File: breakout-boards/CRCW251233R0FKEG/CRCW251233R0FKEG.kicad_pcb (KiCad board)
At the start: 2 copper layers, 14 parts, among them J1 Conn_01x12, J2 Conn_01x12

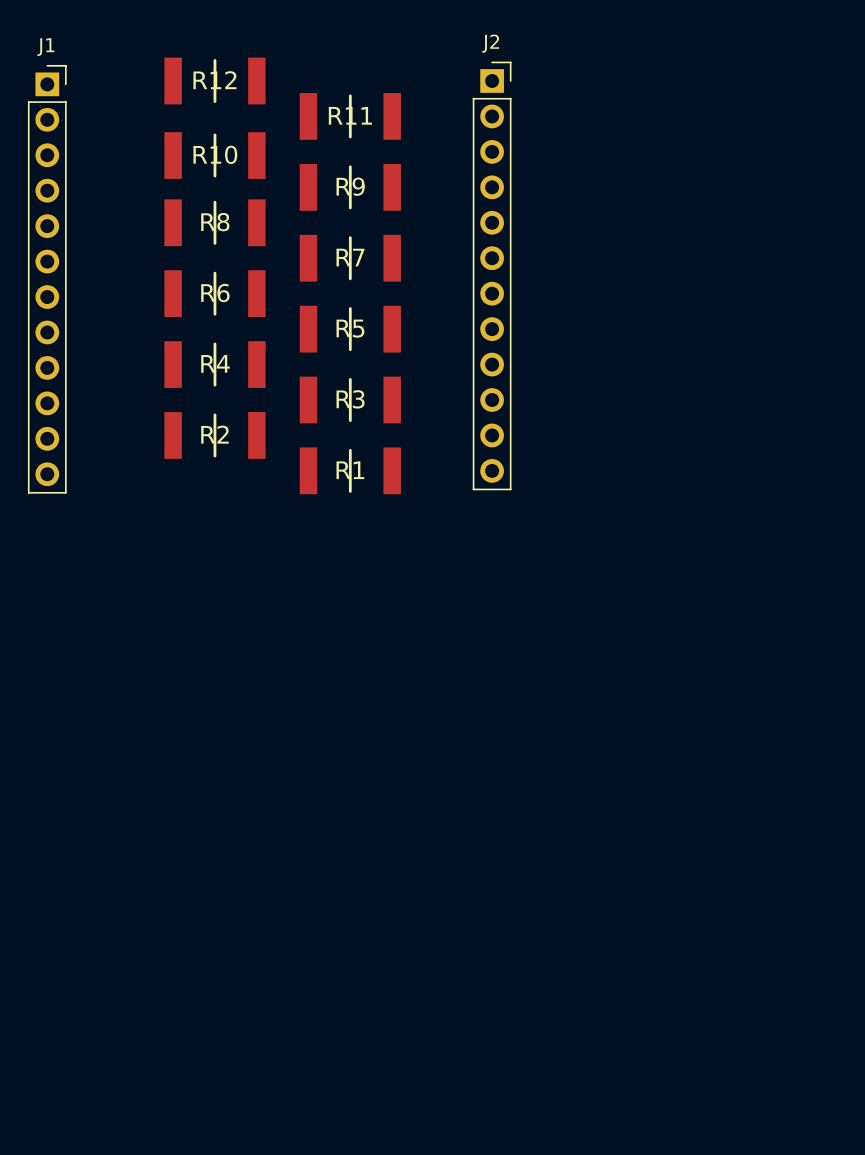
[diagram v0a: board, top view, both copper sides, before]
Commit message: fix: change board alignement
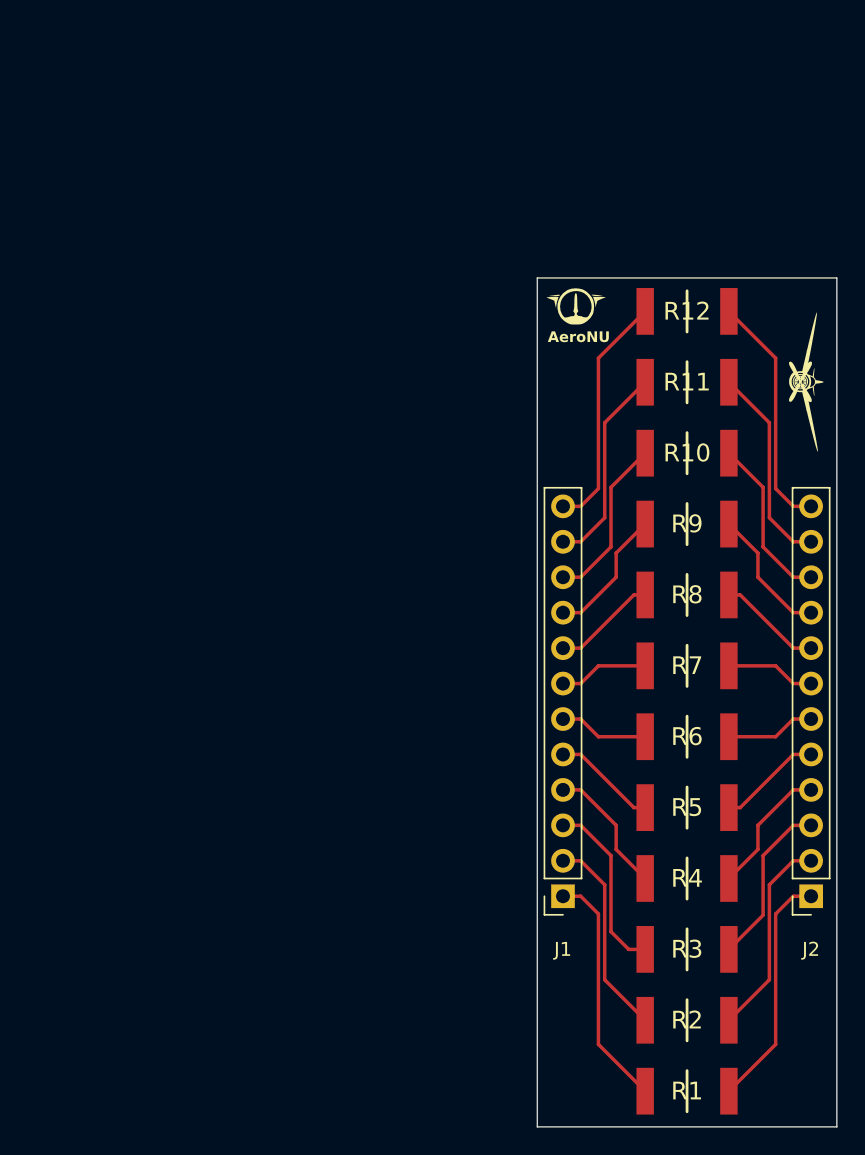
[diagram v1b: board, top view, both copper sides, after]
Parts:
- added AeroNU: LOGO, FixedWing:AeroNU - Logo (Smol), F.Cu at (153.5, 64.6)
- added FixedWing: LOGO, FixedWing:FixedWing - Logo (Smol), F.Cu at (169.2, 67.3)
- moved J1 68.9 mm to (152.4, 104.1), turned to 180 degrees
- moved J2 62.7 mm to (170.2, 104.1), turned to 180 degrees
- moved R2 53.9 mm to (161.3, 113.0)
- moved R1 50.6 mm to (161.3, 118.1)
- moved R4 50.0 mm to (161.3, 102.9)
- moved R6 46.4 mm to (161.3, 92.7)
- moved R3 46.2 mm to (161.3, 108.0)
- moved R8 43.1 mm to (161.3, 82.5)
- moved R5 41.9 mm to (161.3, 97.8)
- moved R10 40.0 mm to (161.3, 72.4)
- moved R7 37.9 mm to (161.3, 87.6)
- moved R12 37.6 mm to (161.3, 62.2)
- moved R9 34.1 mm to (161.3, 77.5)
- moved R11 30.7 mm to (161.3, 67.3)
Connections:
- R1 pad 1: Net-(J1-Pin_12) -> Net-(J1-Pin_1)
- R1 pad 2: Net-(J2-Pin_12) -> Net-(J2-Pin_1)
- R10 pad 1: Net-(J1-Pin_3) -> Net-(J1-Pin_10)
- R10 pad 2: Net-(J2-Pin_3) -> Net-(J2-Pin_10)
- R11 pad 1: Net-(J1-Pin_2) -> Net-(J1-Pin_11)
- R11 pad 2: Net-(J2-Pin_2) -> Net-(J2-Pin_11)
- R12 pad 1: Net-(J1-Pin_1) -> Net-(J1-Pin_12)
- R12 pad 2: Net-(J2-Pin_1) -> Net-(J2-Pin_12)
- R2 pad 1: Net-(J1-Pin_11) -> Net-(J1-Pin_2)
- R2 pad 2: Net-(J2-Pin_11) -> Net-(J2-Pin_2)
- R3 pad 1: Net-(J1-Pin_10) -> Net-(J1-Pin_3)
- R3 pad 2: Net-(J2-Pin_10) -> Net-(J2-Pin_3)
- R4 pad 1: Net-(J1-Pin_9) -> Net-(J1-Pin_4)
- R4 pad 2: Net-(J2-Pin_9) -> Net-(J2-Pin_4)
- R5 pad 1: Net-(J1-Pin_8) -> Net-(J1-Pin_5)
- R5 pad 2: Net-(J2-Pin_8) -> Net-(J2-Pin_5)
- R6 pad 1: Net-(J1-Pin_7) -> Net-(J1-Pin_6)
- R6 pad 2: Net-(J2-Pin_7) -> Net-(J2-Pin_6)
- R7 pad 1: Net-(J1-Pin_6) -> Net-(J1-Pin_7)
- R7 pad 2: Net-(J2-Pin_6) -> Net-(J2-Pin_7)
- R8 pad 1: Net-(J1-Pin_5) -> Net-(J1-Pin_8)
- R8 pad 2: Net-(J2-Pin_5) -> Net-(J2-Pin_8)
- R9 pad 1: Net-(J1-Pin_4) -> Net-(J1-Pin_9)
- R9 pad 2: Net-(J2-Pin_4) -> Net-(J2-Pin_9)
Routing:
- net Net-(J2-Pin_12): track 0.00 -> 17.2 mm
- net Net-(J2-Pin_1): track 0.00 -> 17.2 mm
- net Net-(J1-Pin_12): track 0.00 -> 17.2 mm
- net Net-(J1-Pin_1): track 0.00 -> 17.2 mm
- net Net-(J2-Pin_2): track 0.00 -> 14.6 mm
- net Net-(J2-Pin_11): track 0.00 -> 14.6 mm
- net Net-(J1-Pin_2): track 0.00 -> 14.6 mm
- net Net-(J1-Pin_11): track 0.00 -> 14.6 mm
- net Net-(J1-Pin_3): track 0.00 -> 12.8 mm
- net Net-(J2-Pin_3): track 0.00 -> 12.1 mm
- net Net-(J2-Pin_10): track 0.00 -> 12.1 mm
- net Net-(J1-Pin_10): track 0.00 -> 12.1 mm
- net Net-(J2-Pin_4): track 0.00 -> 9.53 mm
- net Net-(J2-Pin_9): track 0.00 -> 9.53 mm
- net Net-(J1-Pin_4): track 0.00 -> 9.53 mm
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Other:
- board outline added: 21.5 x 60.8 mm
- board text added: "AeroNU"
- board text added: "Designed By Ephram CJ and Matthew F"

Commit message: feat: finalize 33ohm board design
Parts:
- removed the FixedWing at (169.2, 67.3)
- added FixedWing: LOGO, FixedWing Symbols:FixedWing - Logo (Smol), F.Cu at (169.2, 67.1)
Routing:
- net Net-(J2-Pin_12): track 17.2 -> 18.5 mm
- net Net-(J1-Pin_12): track 17.2 -> 18.5 mm
- net Net-(J2-Pin_11): track 14.6 -> 15.9 mm
- net Net-(J2-Pin_3): track 12.1 -> 13.3 mm
- net Net-(J1-Pin_11): track 14.6 -> 15.8 mm
- net Net-(J1-Pin_1): track 17.2 -> 18.4 mm
- net Net-(J2-Pin_10): track 12.1 -> 13.1 mm
- net Net-(J2-Pin_1): track 17.2 -> 18.2 mm
- net Net-(J1-Pin_10): track 12.1 -> 13.1 mm
- net Net-(J1-Pin_2): track 14.6 -> 15.7 mm
- net Net-(J1-Pin_4): track 9.53 -> 10.6 mm
- net Net-(J2-Pin_5): track 7.47 -> 8.51 mm
- net Net-(J2-Pin_2): track 14.6 -> 15.6 mm
- net Net-(J2-Pin_4): track 9.53 -> 10.5 mm
- net Net-(J2-Pin_9): track 9.53 -> 10.5 mm
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
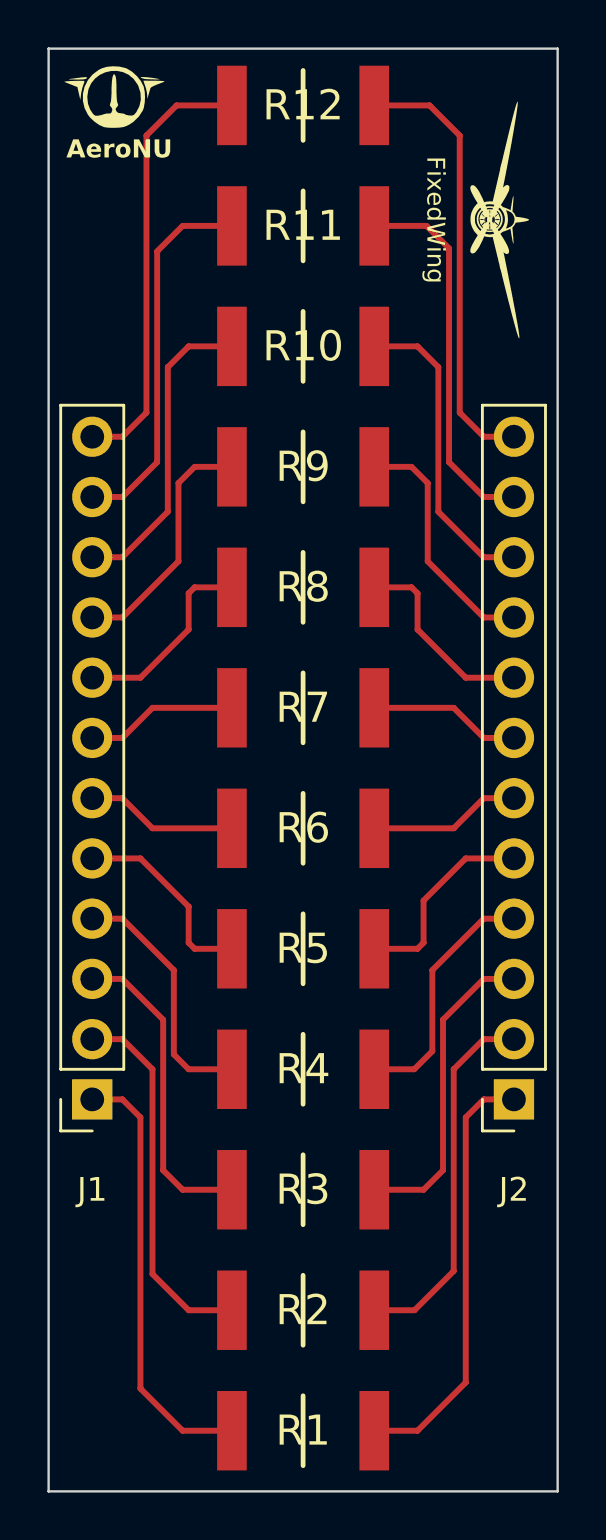
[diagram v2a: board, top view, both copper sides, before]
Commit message: feat: add fillets to all boards
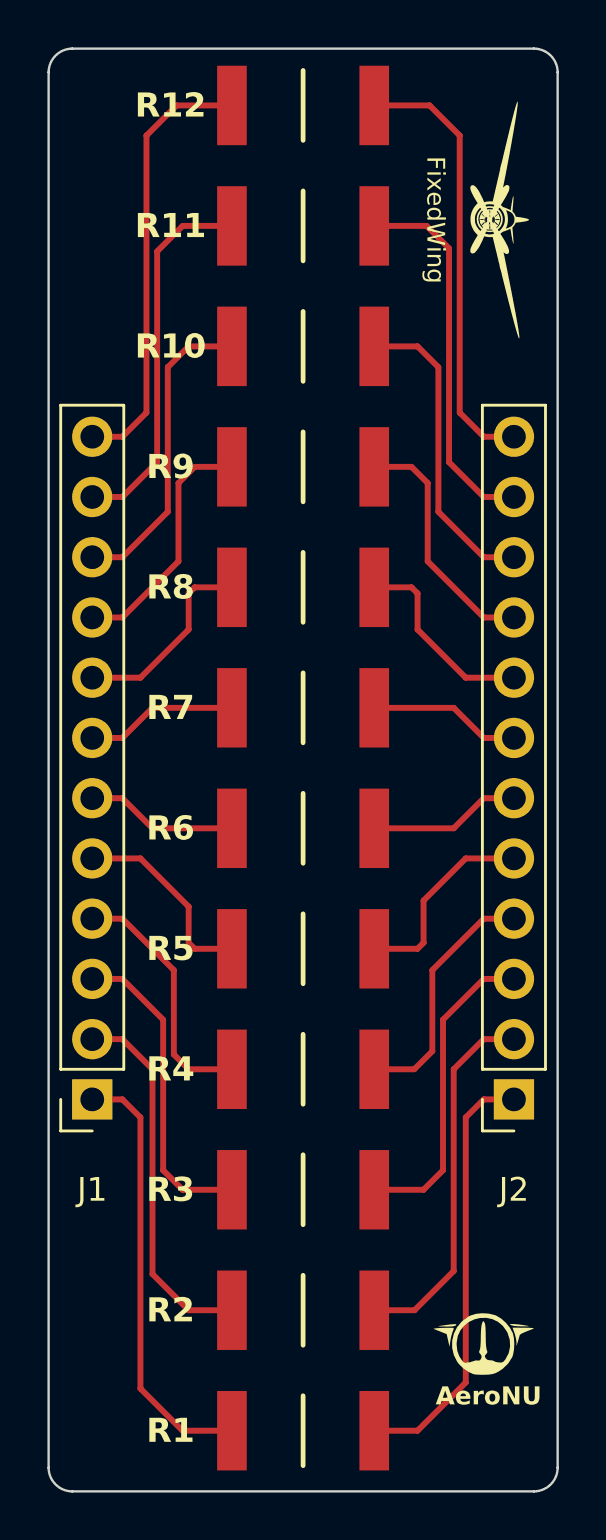
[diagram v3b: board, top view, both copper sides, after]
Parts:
- moved AeroNU 54.8 mm to (169.0, 117.2)
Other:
- outline, holes or cut-outs redrawn
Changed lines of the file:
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@@
       (outputformat 1)
       (mirror false)
-      (drillshape 1)
+      (drillshape 0)
       (scaleselection 1)
       (outputdirectory "")
@@
     (property "ki_description" "Standard Thick Film Chip Resistors value 33R0 ohm.")
     (attr smd)
-    (fp_text reference "R5" (at 0 0) (layer "F.SilkS")
-        (effects (font (size 1.27 1.27) (thickness 0.254)))
+    (fp_text reference "R5" (at -5.588 0) (layer "F.SilkS")
+        (effects (font (size 1.016 1.016) (thickness 0.2032) bold))
     )
     (fp_text value "33Ω" (at 0 0) (layer "F.SilkS") hide
@@
   )
   (footprint "FixedWing:AeroNU - Logo (Smol)" (layer "F.Cu")
-    (at 153.456838 64.647988)
+    (at 169.026549 117.225988)
     (attr board_only exclude_from_pos_files exclude_from_bom)
     (fp_text reference "AeroNU" (at 0 0) (layer "F.SilkS") hide
@@
     (property "ki_description" "Standard Thick Film Chip Resistors value 33R0 ohm.")
     (attr smd)
-    (fp_text reference "R8" (at 0 0) (layer "F.SilkS")
-        (effects (font (size 1.27 1.27) (thickness 0.254)))
+    (fp_text reference "R8" (at -5.588 0) (layer "F.SilkS")
+        (effects (font (size 1.016 1.016) (thickness 0.2032) bold))
     )
     (fp_text value "33Ω" (at 0 0) (layer "F.SilkS") hide
@@
     (property "ki_description" "Standard Thick Film Chip Resistors value 33R0 ohm.")
     (attr smd)
-    (fp_text reference "R9" (at 0 0) (layer "F.SilkS")
-        (effects (font (size 1.27 1.27) (thickness 0.254)))
+    (fp_text reference "R9" (at -5.588 0) (layer "F.SilkS")
+        (effects (font (size 1.016 1.016) (thickness 0.2032) bold))
     )
     (fp_text value "33Ω" (at 0 0) (layer "F.SilkS") hide
@@
     (property "ki_description" "Standard Thick Film Chip Resistors value 33R0 ohm.")
     (attr smd)
-    (fp_text reference "R10" (at 0 0) (layer "F.SilkS")
-        (effects (font (size 1.27 1.27) (thickness 0.254)))
+    (fp_text reference "R10" (at -5.588 0) (layer "F.SilkS")
+        (effects (font (size 1.016 1.016) (thickness 0.2032) bold))
     )
     (fp_text value "33Ω" (at 0 0) (layer "F.SilkS") hide
@@
     (property "ki_description" "Standard Thick Film Chip Resistors value 33R0 ohm.")
     (attr smd)
-    (fp_text reference "R4" (at 0 0) (layer "F.SilkS")
-        (effects (font (size 1.27 1.27) (thickness 0.254)))
+    (fp_text reference "R4" (at -5.588 0) (layer "F.SilkS")
+        (effects (font (size 1.016 1.016) (thickness 0.2032) bold))
     )
     (fp_text value "33Ω" (at 0 0) (layer "F.SilkS") hide
@@
     (property "ki_description" "Standard Thick Film Chip Resistors value 33R0 ohm.")
     (attr smd)
-    (fp_text reference "R2" (at 0 0) (layer "F.SilkS")
-        (effects (font (size 1.27 1.27) (thickness 0.254)))
+    (fp_text reference "R2" (at -5.588 0) (layer "F.SilkS")
+        (effects (font (size 1.016 1.016) (thickness 0.2032) bold))
     )
     (fp_text value "33Ω" (at 0 0) (layer "F.SilkS") hide
@@
     (property "ki_description" "Standard Thick Film Chip Resistors value 33R0 ohm.")
     (attr smd)
-    (fp_text reference "R11" (at 0 0) (layer "F.SilkS")
-        (effects (font (size 1.27 1.27) (thickness 0.254)))
+    (fp_text reference "R11" (at -5.588 0) (layer "F.SilkS")
+        (effects (font (size 1.016 1.016) (thickness 0.2032) bold))
     )
     (fp_text value "33Ω" (at 0 0) (layer "F.SilkS") hide
@@
     (property "ki_description" "Standard Thick Film Chip Resistors value 33R0 ohm.")
     (attr smd)
-    (fp_text reference "R1" (at 0 0) (layer "F.SilkS")
-        (effects (font (size 1.27 1.27) (thickness 0.254)))
+    (fp_text reference "R1" (at -5.588 0) (layer "F.SilkS")
+        (effects (font (size 1.016 1.016) (thickness 0.2032) bold))
     )
     (fp_text value "33Ω" (at 0 0) (layer "F.SilkS") hide
@@
     (property "ki_description" "Standard Thick Film Chip Resistors value 33R0 ohm.")
     (attr smd)
-    (fp_text reference "R3" (at 0 0) (layer "F.SilkS")
-        (effects (font (size 1.27 1.27) (thickness 0.254)))
+    (fp_text reference "R3" (at -5.588 0) (layer "F.SilkS")
+        (effects (font (size 1.016 1.016) (thickness 0.2032) bold))
     )
     (fp_text value "33Ω" (at 0 0) (layer "F.SilkS") hide
@@
     (property "ki_description" "Standard Thick Film Chip Resistors value 33R0 ohm.")
     (attr smd)
-    (fp_text reference "R7" (at 0 0) (layer "F.SilkS")
-        (effects (font (size 1.27 1.27) (thickness 0.254)))
+    (fp_text reference "R7" (at -5.588 0) (layer "F.SilkS")
+        (effects (font (size 1.016 1.016) (thickness 0.2032) bold))
     )
     (fp_text value "33Ω" (at 0 0) (layer "F.SilkS") hide
@@
     (property "ki_description" "Standard Thick Film Chip Resistors value 33R0 ohm.")
     (attr smd)
-    (fp_text reference "R12" (at 0 0) (layer "F.SilkS")
-        (effects (font (size 1.27 1.27) (thickness 0.254)))
+    (fp_text reference "R12" (at -5.588 0) (layer "F.SilkS")
+        (effects (font (size 1.016 1.016) (thickness 0.2032) bold))
     )
     (fp_text value "33Ω" (at 0 0) (layer "F.SilkS") hide
@@
     (property "ki_description" "Standard Thick Film Chip Resistors value 33R0 ohm.")
     (attr smd)
-    (fp_text reference "R6" (at 0 0) (layer "F.SilkS")
-        (effects (font (size 1.27 1.27) (thickness 0.254)))
+    (fp_text reference "R6" (at -5.588 0) (layer "F.SilkS")
+        (effects (font (size 1.016 1.016) (thickness 0.2032) bold))
     )
     (fp_text value "33Ω" (at 0 0) (layer "F.SilkS") hide
@@
     )
   )
-  (gr_rect (start 150.560186 59.834981) (end 172.023186 120.667981)
-    (stroke (width 0.1) (type default)) (fill none) (layer "Edge.Cuts"))
+  (gr_arc (start 151.560186 120.667981) (mid 150.853079 120.375088) (end 150.560186 119.667981)
+    (stroke (width 0.1) (type default)) (layer "Edge.Cuts"))
+  (gr_arc (start 150.560186 60.834981) (mid 150.853085 60.127882) (end 151.560186 59.834981)
+    (stroke (width 0.1) (type default)) (layer "Edge.Cuts"))
+  (gr_line (start 171.023186 120.667981) (end 151.560186 120.667981)
+    (stroke (width 0.1) (type default)) (layer "Edge.Cuts"))
+  (gr_line (start 151.560186 59.834981) (end 171.023186 59.834981)
+    (stroke (width 0.1) (type default)) (layer "Edge.Cuts"))
+  (gr_line (start 150.560186 119.667981) (end 150.560186 60.834981)
+    (stroke (width 0.1) (type default)) (layer "Edge.Cuts"))
+  (gr_line (start 172.023186 60.834981) (end 172.023186 119.667981)
+    (stroke (width 0.1) (type default)) (layer "Edge.Cuts"))
+  (gr_arc (start 172.023186 119.667981) (mid 171.730299 120.375095) (end 171.023186 120.667981)
+    (stroke (width 0.1) (type default)) (layer "Edge.Cuts"))
+  (gr_arc (start 171.023186 59.834981) (mid 171.730293 60.127874) (end 172.023186 60.834981)
+    (stroke (width 0.1) (type default)) (layer "Edge.Cuts"))
   (gr_text "Designed By\nEphram CJ and Matthew F" (at 161.29 119.38) (layer "B.SilkS")
     (effects (font (size 0.762 0.762) (thickness 0.127) bold) (justify bottom mirror))
   )
-  (gr_text "AeroNU" (at 151.308289 64.516) (layer "F.SilkS")
+  (gr_text "AeroNU" (at 166.878 117.094) (layer "F.SilkS")
     (effects (font (size 0.762 0.762) (thickness 0.127) bold) (justify left bottom))
   )
